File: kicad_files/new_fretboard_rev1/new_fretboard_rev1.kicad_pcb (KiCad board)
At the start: 2 copper layers, 576.1 x 81.9 mm, 302 parts, among them J1 530470410, J10 530470410, J11 110990030, J12 110990030, J13 110990030, J14 Conn_01x05, J15 Conn_01x02_Pin, J16 Conn_01x02_Pin, J17 Conn_01x02_Pin, J2 530470410, J3 FTSH-107-01-L-DV-K-A, J4 530470410, J5 530470410, J6 530470410, J7 530470410, J8 530470410, J9 530470410, U1 LX3302AQPW-TR-EASY, U10 STM32F730V8Tx, U11 MIC5504-3.3YM5, U2 LX3302AQPW-TR-EASY, U3 LX3302AQPW-TR-EASY, U4 LX3302AQPW-TR-EASY, U5 LX3302AQPW-TR-EASY, U6 LX3302AQPW-TR-EASY, U7 LX3302AQPW-TR-EASY, U8 LX3302AQPW-TR-EASY, U9 LX3302AQPW-TR-EASY, Y1 ASE-25.000MHZ-LC-T

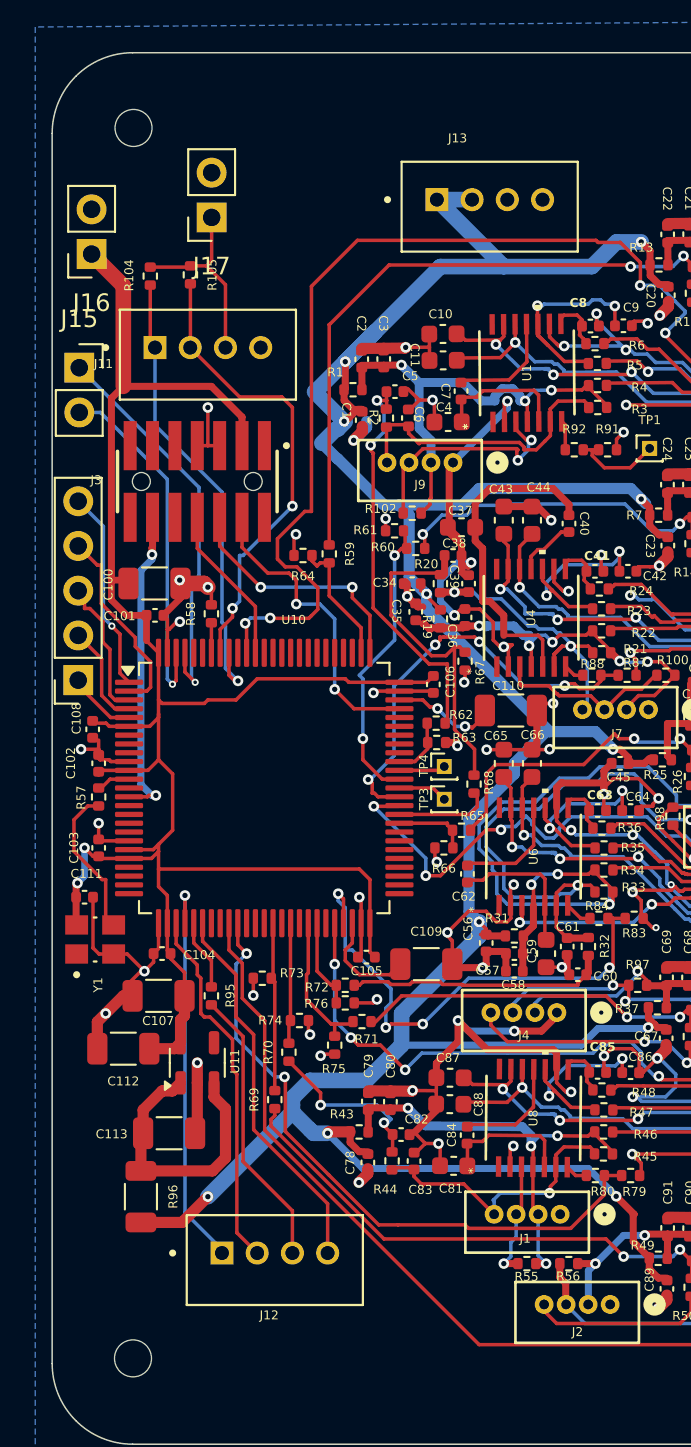
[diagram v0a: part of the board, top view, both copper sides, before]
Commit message: almost done with circuits, changing sd card reader
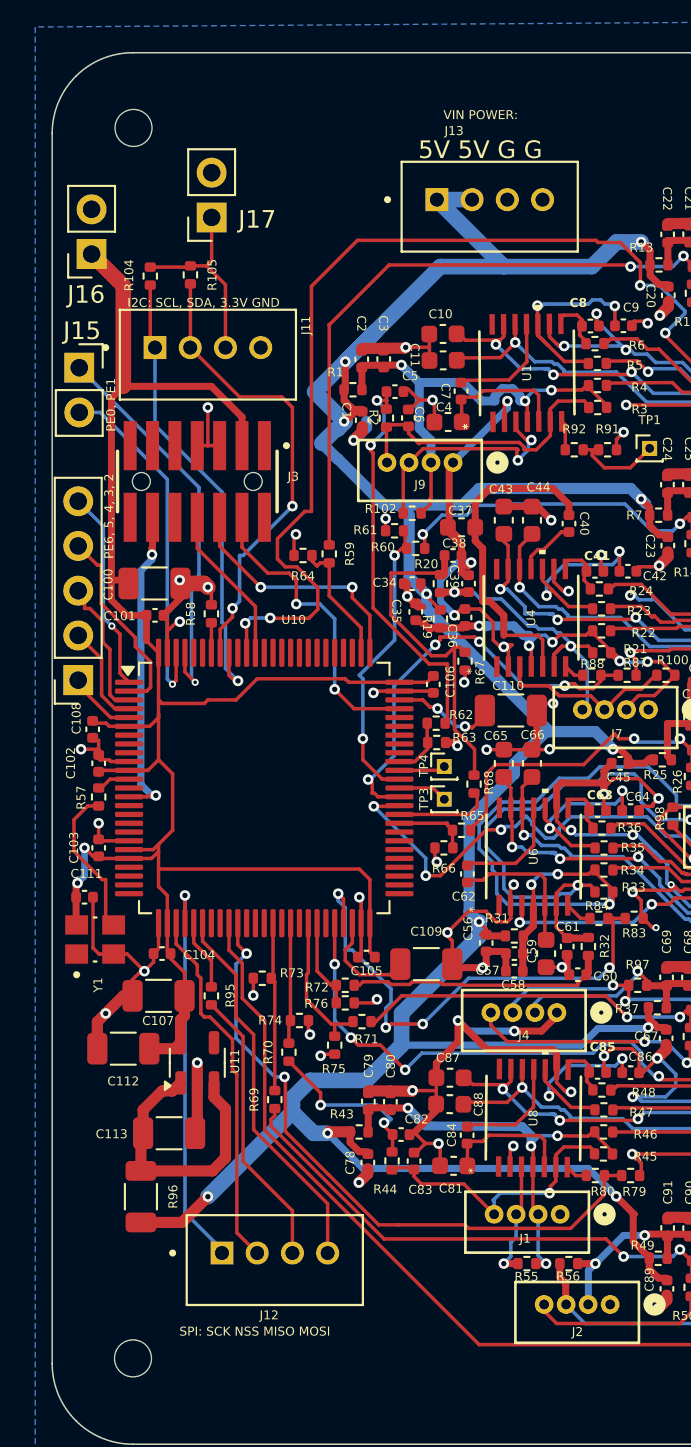
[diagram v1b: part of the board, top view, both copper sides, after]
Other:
- board text added: "5V 5V G G"
- board text added: "I2C: SCL, SDA, 3.3V GND"
- board text added: "PE0, PE1"
- board text added: "PE6, 5, 4, 3, 2"
- board text added: "SPI: SCK NSS MISO MOSI"
- board text added: "VIN POWER:"
